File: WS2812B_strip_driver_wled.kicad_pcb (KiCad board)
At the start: 2 copper layers, 112.9 x 106.2 mm, 119 parts, among them J1 CH_1, J2 CH_2, J3 CH_3, J4 CH_4, J5 PWR_IN, J6 uPhone, J8 USB_C_Receptacle_USB2.0_16P, K1 RELAY_1, K2 RELAY_2, K3 RELAY_3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

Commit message: cleaned up schematic. assigned esp32e as my custom version with 0.3mm vias to stop drc warnings
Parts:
- R41: value 170 -> 170R
- U1: footprint RF_Module:ESP32-WROOM-32E -> JIMS_MCUS:ESP32-WROOM-32E-0.3VIAS
- moved D1 149.5 mm to (260.1, 72.7)
- moved TP_CH2 149.5 mm to (260.4, 86.0)
- moved C10 149.5 mm to (254.2, 110.9)
- moved C11 149.5 mm to (254.2, 134.7)
- moved C12 149.5 mm to (254.2, 87.2)
- moved C2 149.5 mm to (175.5, 63.2)
- moved C4 149.5 mm to (169.3, 135.6)
- moved C5 149.5 mm to (195.2, 65.9)
- moved C6 149.5 mm to (197.4, 65.9)
- moved C8 149.5 mm to (201.7, 93.4)
- moved D10 149.5 mm to (190.6, 112.4)
- moved D11 149.5 mm to (201.4, 64.1)
- moved D2 149.5 mm to (260.3, 97.2)
- moved D3 149.5 mm to (260.3, 120.7)
- moved D4 149.5 mm to (260.3, 144.4)
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
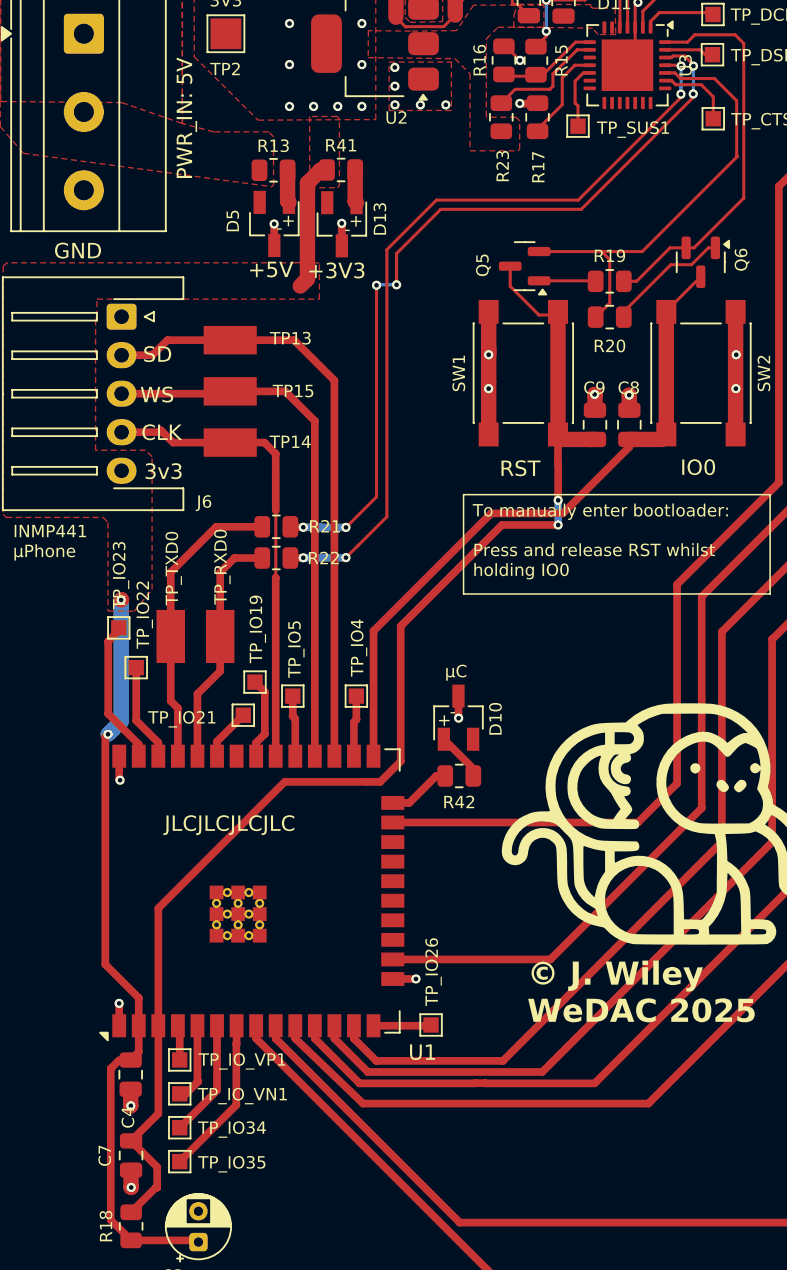
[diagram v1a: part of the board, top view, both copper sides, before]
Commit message: swapped incorrect rx/tx pins
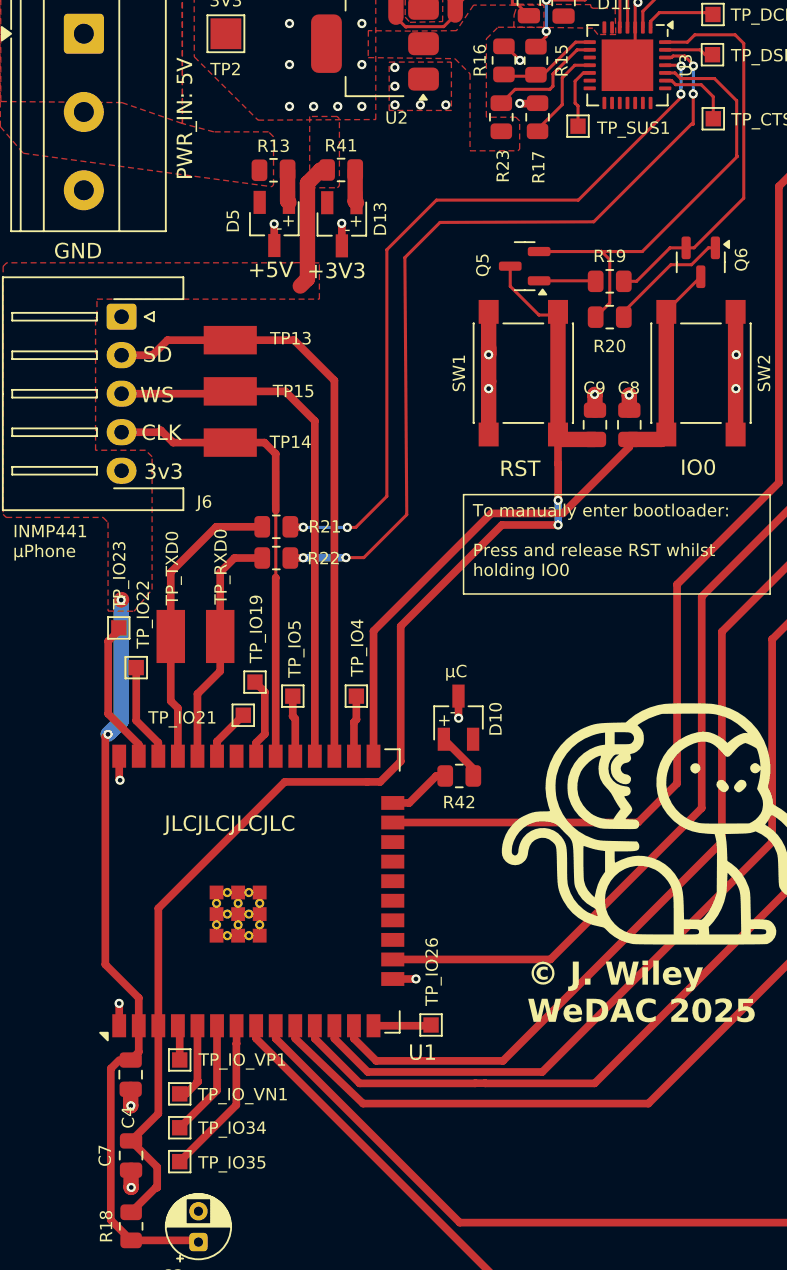
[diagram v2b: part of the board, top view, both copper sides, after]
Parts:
- R1, R2, R3, R4: value 220 -> 270R
- R10, R9: value 170R -> 150R
- R11, R12, R13: value 170 -> 150R
- R15: value 47K5 -> 51K
- R16: value 22K1 -> 27K
- R41, R42: value 170R -> 68R
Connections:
- R21 pad 2: TXD -> RXD
- R22 pad 2: RXD -> TXD
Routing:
- net TXD: track 51.2 -> 53.7 mm, vias 6 -> 4
- net RXD: track 51.0 -> 49.4 mm

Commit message: swapped change en rc circuit vals, removed io btn debouncing cap. Board now fires straight up
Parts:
- removed C8: 0.1uF, Capacitor_SMD:C_0805_2012Metric
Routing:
- net GND: track 54.1 -> 53.1 mm, vias 43 -> 42

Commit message: swapped change en rc circuit vals, removed io btn debouncing cap. Board now fires straight up
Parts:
- C7: value 0.1uF -> 1uF
- R18: value 10K -> 51K
